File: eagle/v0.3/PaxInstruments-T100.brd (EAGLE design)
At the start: 45.1 x 17.1 mm, 29 parts, among them U1 Attiny85

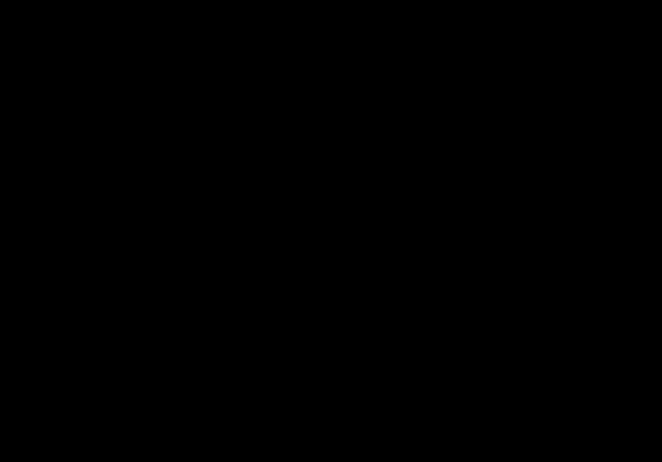
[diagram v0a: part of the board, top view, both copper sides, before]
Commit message: Added indicator LED and breakout header.
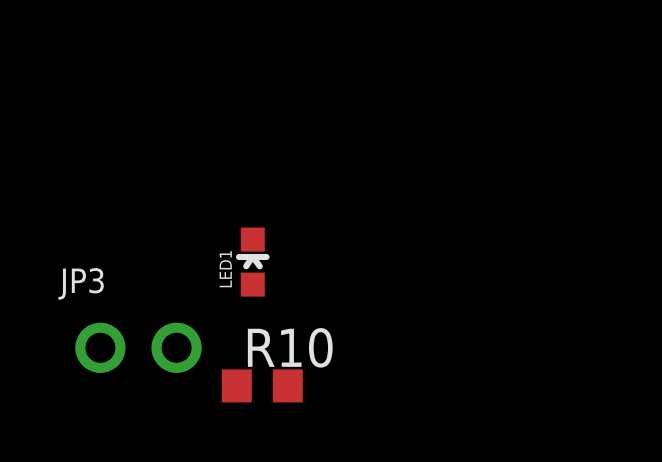
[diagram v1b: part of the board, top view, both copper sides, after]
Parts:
- added JP3: (no value), microbuilder:1X02_ROUND
- added LED1: (no value), SparkFun-LED:LED-0603
- added R10: 500R, rcl:R0603
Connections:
- new net N$5: LED1.A, R10.1
- net GND: now also JP3.1, LED1.C
- net SPARE: now also JP3.2, R10.2
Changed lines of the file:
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@@
 <attribute name="VALUE" x="23.5776" y="15.875" size="0.02" layer="27"/>
 </element>
+<element name="LED1" library="SparkFun-LED" package="LED-0603" value="" x="-16.8275" y="0.9525"/>
+<element name="R10" library="rcl" package="R0603" value="500R" x="-16.51" y="-3.175"/>
+<element name="JP3" library="microbuilder" package="1X02_ROUND" value="" x="-20.6375" y="-1.905"/>
 </elements>
 <signals>
@@
 <contactref element="JP2" pad="6"/>
 <contactref element="SJ1" pad="1"/>
+<contactref element="LED1" pad="C"/>
+<contactref element="JP3" pad="1"/>
+<wire x1="21.2725" y1="11.9625" x2="22.4155" y2="15.875" width="0" layer="19" extent="1-1"/>
+<wire x1="17.8435" y1="10.16" x2="21.2725" y2="11.9625" width="0" layer="19" extent="1-1"/>
+<wire x1="9.7225" y1="8.5725" x2="17.8435" y2="10.16" width="0" layer="19" extent="1-1"/>
+<wire x1="9.7225" y1="12.3825" x2="9.7225" y2="8.5725" width="0" layer="19" extent="1-1"/>
+<wire x1="5.2575" y1="12.0725" x2="9.7225" y2="12.3825" width="0" layer="19" extent="1-1"/>
+<wire x1="12.1793" y1="3.81" x2="9.7225" y2="8.5725" width="0" layer="19" extent="1-1"/>
+<wire x1="9.02" y1="1.905" x2="12.1793" y2="3.81" width="0" layer="19" extent="1-1"/>
+<wire x1="-16.8275" y1="1.7025" x2="5.2575" y2="12.0725" width="0" layer="19" extent="1-1"/>
+<wire x1="-21.9075" y1="-1.905" x2="-16.8275" y2="1.7025" width="0" layer="19" extent="1-1"/>
 </signal>
 <signal name="/RST">
@@
 <wire x1="14.2875" y1="13.97" x2="14.2875" y2="15.24" width="0.254" layer="1"/>
 <wire x1="14.2875" y1="15.24" x2="13.2715" y2="15.24" width="0.254" layer="1"/>
+<contactref element="R10" pad="2"/>
+<contactref element="JP3" pad="2"/>
+<wire x1="-15.66" y1="-3.175" x2="14.2875" y2="5.08" width="0" layer="19" extent="1-1"/>
+<wire x1="-19.3675" y1="-1.905" x2="-15.66" y2="-3.175" width="0" layer="19" extent="1-1"/>
 </signal>
 <signal name="SDA">
@@
 <wire x1="37.846" y1="12.3825" x2="38.1" y2="12.6365" width="0.4064" layer="1"/>
 </signal>
+<signal name="N$5">
+<contactref element="R10" pad="1"/>
+<contactref element="LED1" pad="A"/>
+<wire x1="-16.8275" y1="0.2025" x2="-17.36" y2="-3.175" width="0" layer="19" extent="1-1"/>
+</signal>
 </signals>

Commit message: [V0.3] - initial layout
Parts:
- removed LOGO1: OSHW-LOGOS, SparkFun-Aesthetics:OSHW-LOGO-S
- removed SJ1: (no value), jumper:SJ
- removed U$1: PAX-LOGO, charlespax:PAX-LOGO
- removed U$2: CHARLESPAX_TC-MINI-CONNECTOR, PaxInstrument-T400:CHARLESPAX_TC-MINI-CONNECTOR
- added L2: (no value), SeeesStudio-OPL:L0603
- added U$5: TC-MINI-INSIDE, PaxInstruments-Connectors:TC-CLIP-INSIDE
- moved JP3 33.3 mm to (7.94, 15.2)
- moved R10 29.7 mm to (12.7, 2.22)
- moved LED1 29.5 mm to (12.7, 0.95), turned to 90 degrees
- moved C6 1.59 mm to (29.8, 4.13)
- moved R3 1.59 mm to (29.8, 5.71)
- moved U$4 0.64 mm to (26.0, 12.7)
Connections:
- net AGND: now also L2.2; no longer SJ1.2
- net GND: now also L2.1; no longer SJ1.1
- net N$3: now also U$5.P$2; no longer U$2.P$2
- net N$4: now also U$5.P$1; no longer U$2.P$1
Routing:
- net SPARE: track 15.8 -> 22.9 mm
- net D+: track 15.5 -> 8.89 mm, vias 2 -> 0
- net N$4: track 14.1 -> 10.3 mm
- net SDA: track 35.4 -> 31.7 mm
- net N$5: track 0.00 -> 2.05 mm
- net USB_5V: track 71.4 -> 69.5 mm, vias 3 -> 2
- net TC-: track 7.12 -> 8.86 mm
- net A_5V: track 27.4 -> 28.9 mm
- net N$3: track 13.6 -> 12.4 mm
- net SCL: track 21.8 -> 21.0 mm
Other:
- board size 45.1 x 17.1 mm -> 46 x 17.1 mm
- board text added: "LOGO"

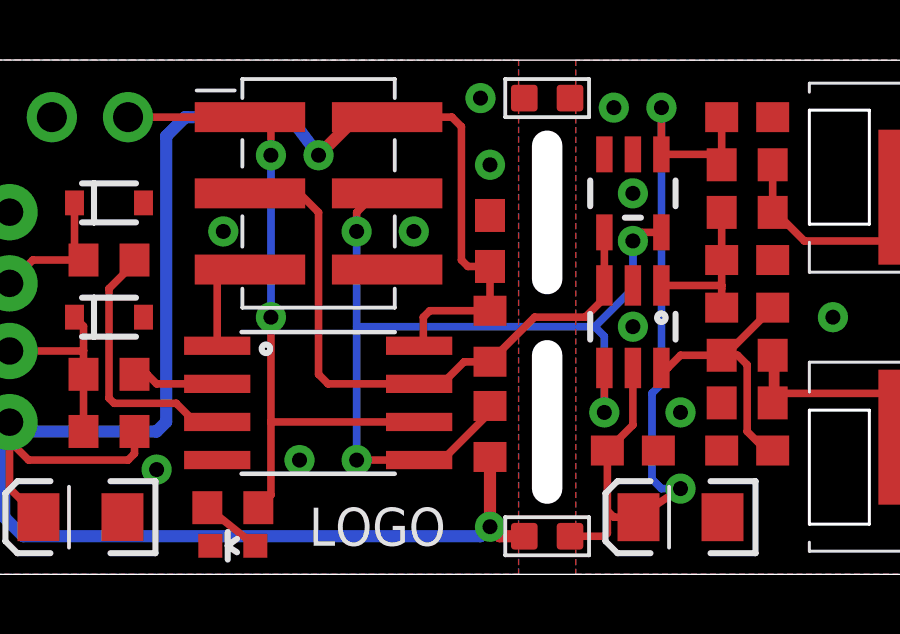
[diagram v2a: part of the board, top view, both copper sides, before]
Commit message: New library added. Inductor changed to resistor. Logo placement.
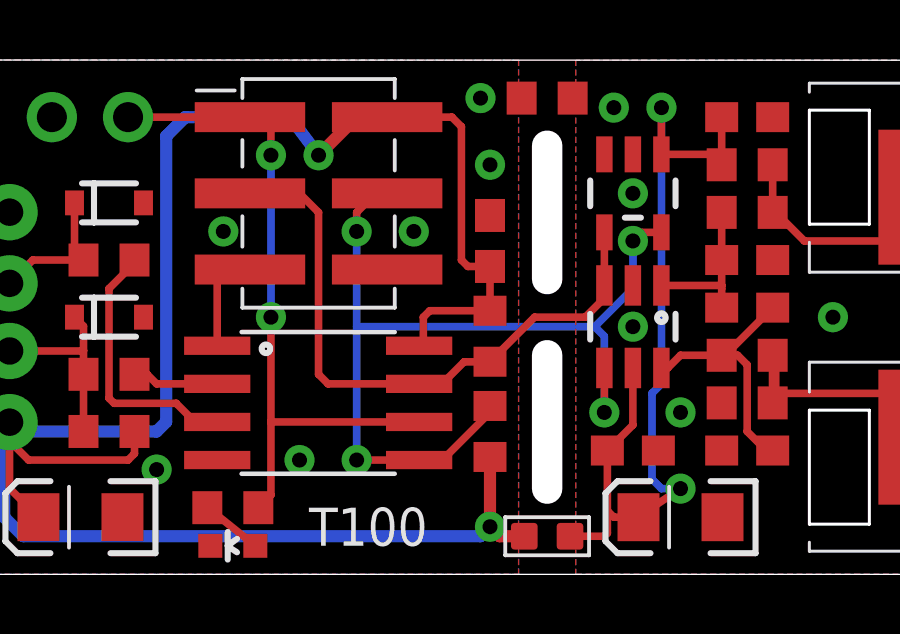
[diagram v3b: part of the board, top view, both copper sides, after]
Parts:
- removed L2: (no value), SeeesStudio-OPL:L0603
- added R11: 0R, rcl:R0603
- added U$1: PAX-LOGOPAX-LOGO-0.25IN, PaxInstruments-Aesthetics:PAX-LOGO-0.25IN
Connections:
- net AGND: now also R11.1; no longer L2.2
- net GND: now also R11.2; no longer L2.1
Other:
- board text added: "T100"
- board text removed: "LOGO"
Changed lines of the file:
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@@
 <text x="45.085" y="18.415" size="1.016" layer="26" font="vector" rot="MR0">Pax Instruments T-100
 [v0.3] x 2014</text>
-<text x="15.24" y="0.9525" size="1.27" layer="25" font="vector">LOGO</text>
+<text x="15.24" y="0.9525" size="1.27" layer="25" font="vector">T100</text>
 </plain>
 <attributes>
@@
 <attribute name="MPN" value="Thermo-clip2" x="38.4175" y="8.5725" size="1.778" layer="27" rot="R270" display="off"/>
 </element>
-<element name="L2" library="SeeesStudio-OPL" package="L0603" value="" x="23.1775" y="15.875" smashed="yes">
-<attribute name="VALUE" x="21.6535" y="15.5575" size="0.635" layer="27" ratio="10"/>
-</element>
+<element name="U$1" library="PaxInstruments-Aesthetics" package="PAX-LOGO-0.25IN" value="PAX-LOGOPAX-LOGO-0.25IN" x="13.0175" y="4.1275" rot="MR0"/>
+<element name="R11" library="rcl" package="R0603" value="0R" x="23.1775" y="15.875" smashed="yes" rot="R180"/>
 </elements>
 <signals>
@@
 <contactref element="LED1" pad="C"/>
 <contactref element="JP3" pad="1"/>
-<contactref element="L2" pad="1"/>
 <via x="18.7325" y="11.43" extent="1-16" drill="0.5"/>
 <via x="21.2725" y="13.6525" extent="1-16" drill="0.5"/>
@@
 <via x="10.16" y="3.4925" extent="1-16" drill="0.5"/>
 <via x="14.9225" y="3.81" extent="1-16" drill="0.5"/>
+<contactref element="R11" pad="2"/>
 </signal>
 <signal name="/RST">
@@
 <contactref element="C6" pad="2"/>
 <contactref element="C7" pad="2"/>
-<contactref element="L2" pad="2"/>
 <via x="43.815" y="8.5725" extent="1-16" drill="0.5"/>
 <via x="26.035" y="12.7" extent="1-16" drill="0.5"/>
@@
 <via x="32.7025" y="8.5725" extent="1-16" drill="0.5"/>
 <via x="38.4175" y="8.5725" extent="1-16" drill="0.5"/>
+<contactref element="R11" pad="1"/>
 </signal>
 <signal name="TC+">

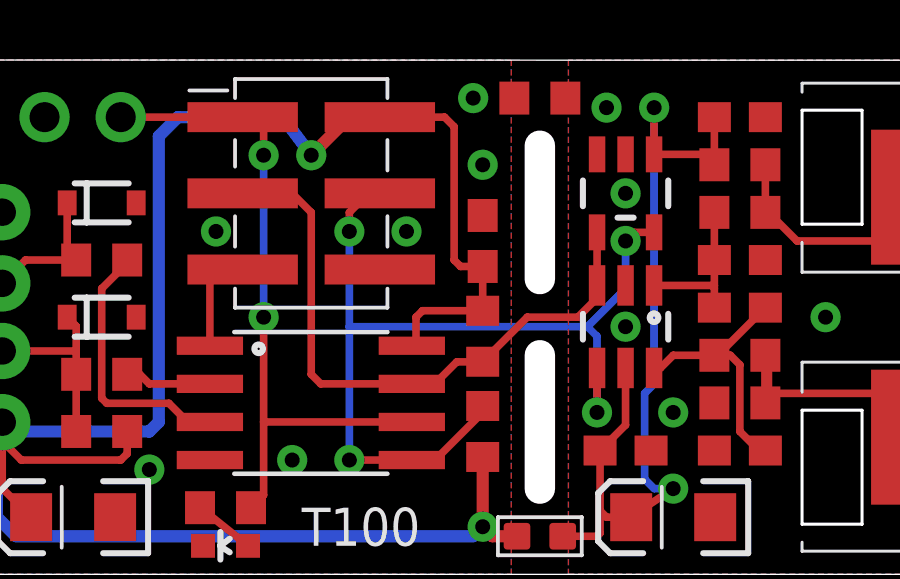
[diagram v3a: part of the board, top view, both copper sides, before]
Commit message: Text label placements.
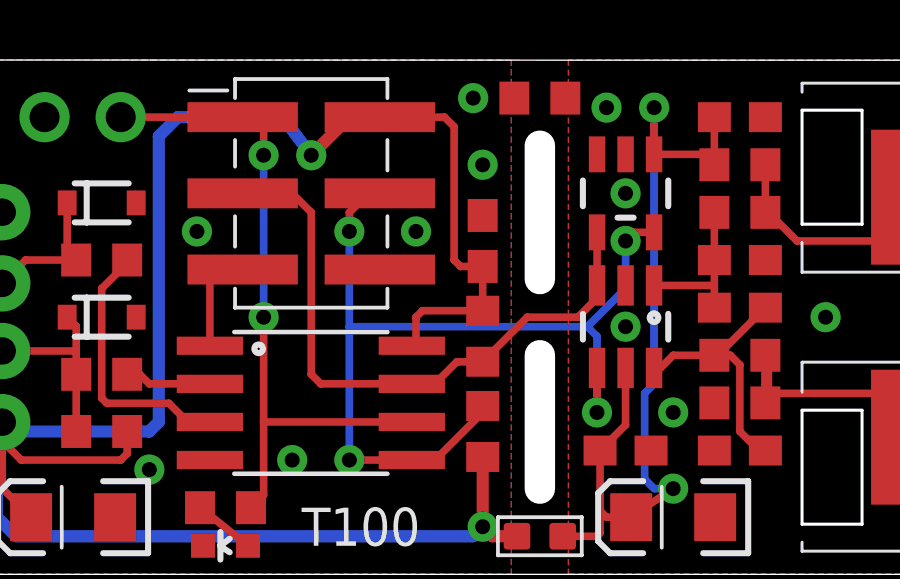
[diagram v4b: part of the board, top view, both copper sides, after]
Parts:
- added LOGO1: SPARKFUN-AESTHETICS_OSHW-LOGOS, PaxInstrument-T400:SPARKFUN-AESTHETICS_OSHW-LOGO-S
- moved U$1 9.34 mm to (20.6, 9.53)
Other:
- board text added: "Pax Instruments Temperature LabStick T100 v0.3 beta"
- board text added: "paxinstruments.com/ products/sku2252"
- board text removed: "Pax Instruments T-100 [v0.3] x 2014"
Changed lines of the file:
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@@
 <wire x1="23.1775" y1="14.2875" x2="23.1775" y2="9.8425" width="1.016" layer="46"/>
 <wire x1="23.1775" y1="7.3025" x2="23.1775" y2="2.8575" width="1.016" layer="46"/>
-<text x="45.085" y="18.415" size="1.016" layer="26" font="vector" rot="MR0">Pax Instruments T-100
-[v0.3] x 2014</text>
+<text x="20.6375" y="4.445" size="0.889" layer="26" font="vector" rot="MR0">Pax Instruments
+Temperature LabStick
+T100 v0.3 beta</text>
 <text x="15.24" y="0.9525" size="1.27" layer="25" font="vector">T100</text>
+<text x="20.6375" y="0.635" size="0.889" layer="26" font="vector" rot="MR0">paxinstruments.com/
+products/sku2252</text>
 </plain>
 <attributes>
@@
 <attribute name="MPN" value="Thermo-clip2" x="38.4175" y="8.5725" size="1.778" layer="27" rot="R270" display="off"/>
 </element>
-<element name="U$1" library="PaxInstruments-Aesthetics" package="PAX-LOGO-0.25IN" value="PAX-LOGOPAX-LOGO-0.25IN" x="13.0175" y="4.1275" rot="MR0"/>
+<element name="U$1" library="PaxInstruments-Aesthetics" package="PAX-LOGO-0.25IN" value="PAX-LOGOPAX-LOGO-0.25IN" x="20.6375" y="9.525" rot="MR0"/>
 <element name="R11" library="rcl" package="R0603" value="0R" x="23.1775" y="15.875" smashed="yes" rot="R180"/>
+<element name="LOGO1" library="PaxInstrument-T400" package="SPARKFUN-AESTHETICS_OSHW-LOGO-S" value="SPARKFUN-AESTHETICS_OSHW-LOGOS" x="38.4175" y="4.445" rot="MR0"/>
 </elements>
 <signals>
@@
 <contactref element="LED1" pad="C"/>
 <contactref element="JP3" pad="1"/>
-<via x="18.7325" y="11.43" extent="1-16" drill="0.5"/>
+<via x="19.05" y="11.43" extent="1-16" drill="0.5"/>
 <via x="21.2725" y="13.6525" extent="1-16" drill="0.5"/>
 <via x="20.955" y="15.875" extent="1-16" drill="0.5"/>
-<via x="12.3825" y="11.43" extent="1-16" drill="0.5"/>
+<via x="11.7475" y="11.43" extent="1-16" drill="0.5"/>
 <via x="10.16" y="3.4925" extent="1-16" drill="0.5"/>
 <via x="14.9225" y="3.81" extent="1-16" drill="0.5"/>
@@
 <contactref element="C7" pad="1"/>
 <wire x1="28.995" y1="12.065" x2="28.995" y2="10.4775" width="0.254" layer="1"/>
-<wire x1="28.995" y1="8.89" x2="28.995" y2="9.525" width="0.254" layer="1"/>
+<wire x1="28.995" y1="8.89" x2="28.995" y2="9.6301" width="0.254" layer="1"/>
 <wire x1="28.995" y1="9.6301" x2="28.995" y2="10.4775" width="0.254" layer="1"/>
 <wire x1="26.985" y1="9.6301" x2="28.995" y2="9.6301" width="0.254" layer="1"/>
-<wire x1="28.995" y1="9.6301" x2="28.995" y2="9.525" width="0.254" layer="1"/>
 </signal>
 <signal name="TC-">

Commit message: Added MCP9800A0 part number. Closes #47.
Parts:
- U$4: value MCP9800 -> MCP9800A0
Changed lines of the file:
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@@
 <?xml version="1.0" encoding="utf-8"?>
 <!DOCTYPE eagle SYSTEM "eagle.dtd">
-<eagle version="7.3.0">
+<eagle version="7.2.0">
 <drawing>
 <settings>
@@
 </element>
 <element name="U$3" library="SparkFun-DigitalIC" package="SOT23-6" value="MCP3421" x="26.035" y="8.255" smashed="yes" rot="R180"/>
-<element name="U$4" library="SparkFun-DigitalIC" package="SOT23-5" value="MCP9800" x="26.035" y="12.7" smashed="yes" rot="R180"/>
+<element name="U$4" library="SparkFun-DigitalIC" package="SOT23-5" value="MCP9800A0" x="26.035" y="12.7" smashed="yes" rot="R180"/>
 <element name="L1" library="SeeesStudio-OPL" package="L0603" value="" x="23.1775" y="1.27" smashed="yes">
 <attribute name="VALUE" x="21.6535" y="0.9525" size="0.635" layer="27" ratio="10"/>

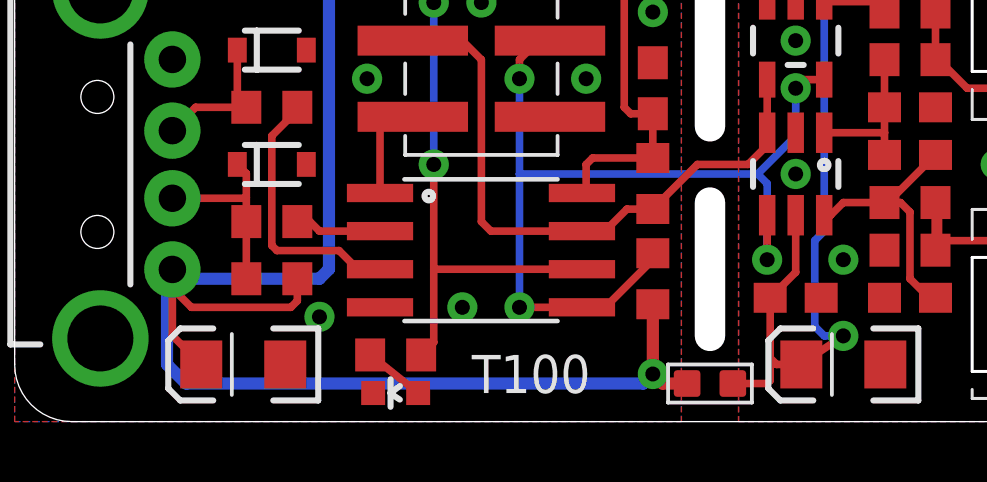
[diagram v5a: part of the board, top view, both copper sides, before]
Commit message: Added a bunch of BoM data.
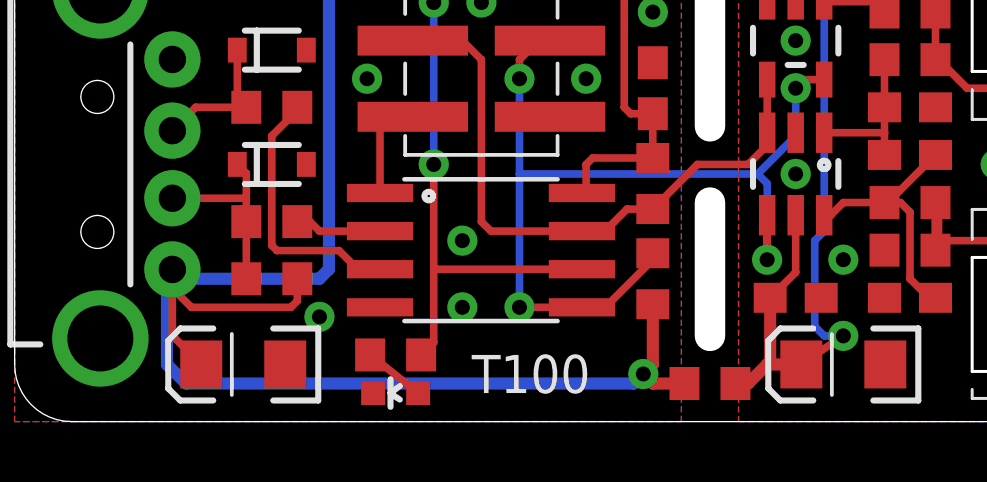
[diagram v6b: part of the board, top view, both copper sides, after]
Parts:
- removed L1: (no value), SeeesStudio-OPL:L0603
- removed LOGO1: SPARKFUN-AESTHETICS_OSHW-LOGOS, PaxInstrument-T400:SPARKFUN-AESTHETICS_OSHW-LOGO-S
- added R12: 0R, rcl:R0603
- LED1: value (none) -> Green
- U$3: value MCP3421 -> MCP3421A0
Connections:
- net A_5V: now also R12.1; no longer L1.2
- net USB_5V: now also R12.2; no longer L1.1

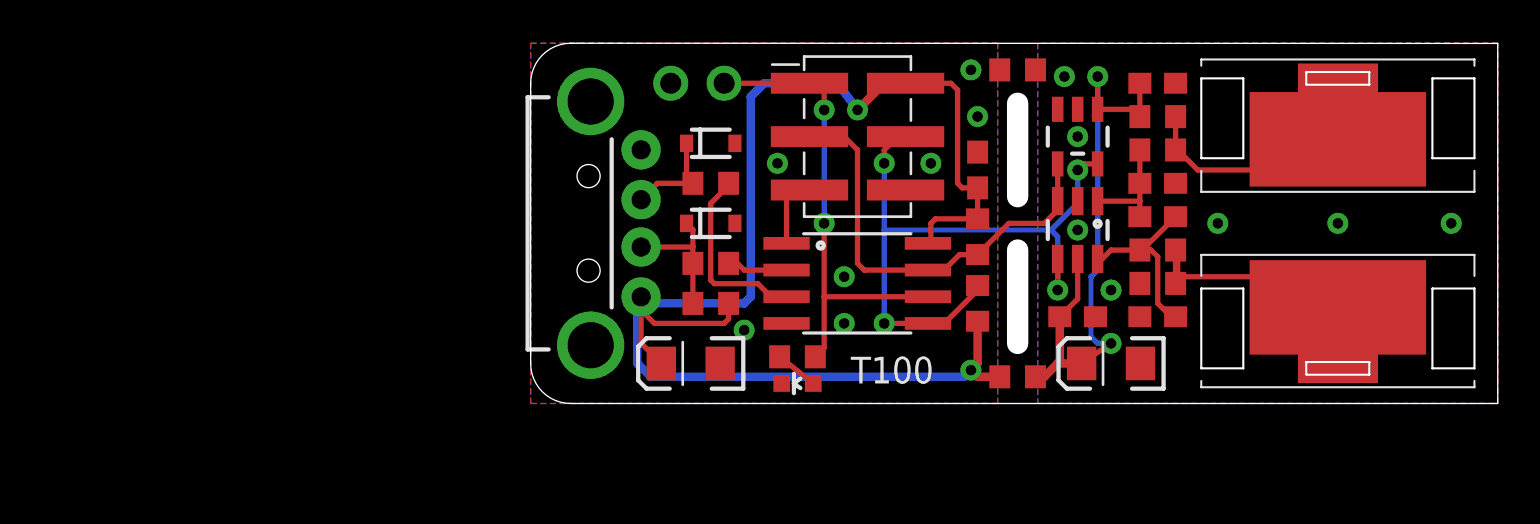
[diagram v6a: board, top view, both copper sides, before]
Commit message: Updated thermocoupel connector. Moved MCP9800 to between the thermocouple connectors. BoM should be finished.
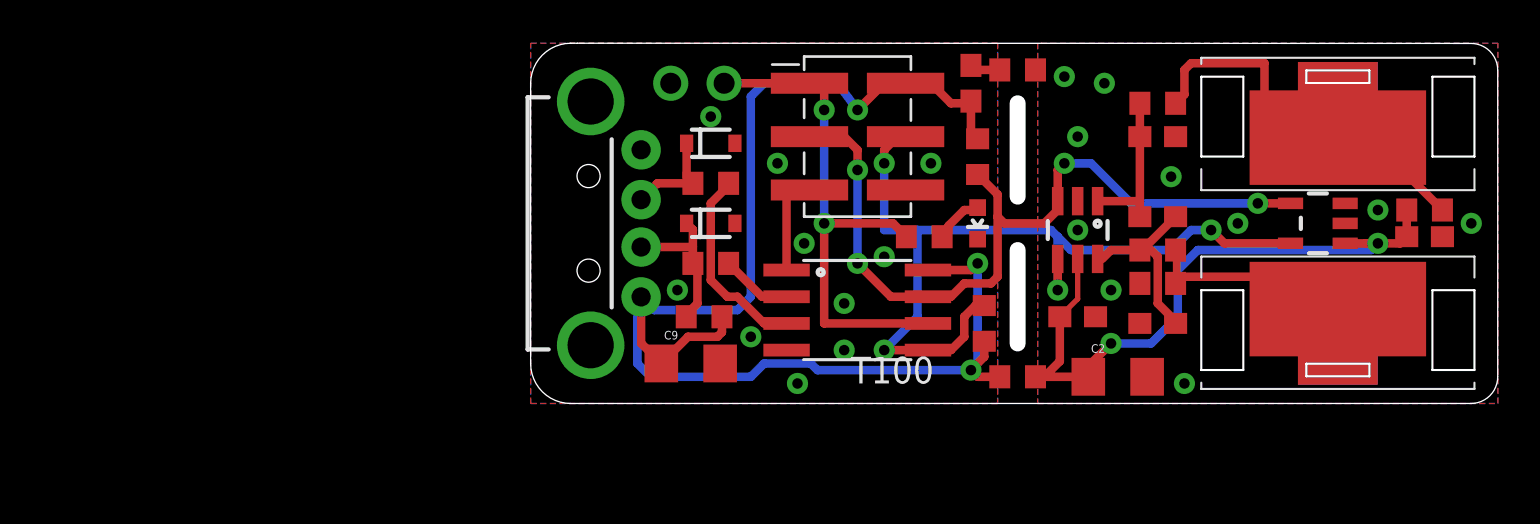
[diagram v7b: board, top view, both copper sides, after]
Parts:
- removed C3: 10uF, SparkFun-Capacitors:EIA3216
- removed U$5: TC-MINI-INSIDE, PaxInstruments-Connectors:TC-CLIP-INSIDE
- added C9: 10uF, SparkFun-Passives:1206
- added U$2, U$6: TC-MINI-SINGLE, PaxInstruments-Connectors:TC-CLIP-SINGLE
- C2: device SparkFun-Capacitors:EIA3216 -> SparkFun-Passives:1206
- R10, R5, R6: value 500R -> 499R
- moved C2 20.3 mm to (27.9, 1.27), turned to 0 degrees
- moved C5 14.6 mm to (42.5, 7.94)
- moved R4 13.5 mm to (42.5, 9.21)
- moved U$4 12.2 mm to (37.5, 8.57), turned to 90 degrees
- moved LED1 11.5 mm to (21.3, 8.57), turned to 180 degrees
- moved R10 8.31 mm to (18.7, 7.94), turned to 180 degrees
- moved C1 4.14 mm to (21.0, 15.2)
- moved R8 3.81 mm to (21.3, 11.7)
- moved C7 2.22 mm to (29.8, 12.7)
- moved R6 2.22 mm to (29.8, 14.3)
- moved U1 1.27 mm to (15.6, 4.45)
- moved R7 1.00 mm to (21.6, 3.81)
- moved R9 0.71 mm to (8.26, 4.13)
- moved C6 0.32 mm to (29.8, 3.81)
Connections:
- net AGND: now also C2.2; no longer C3.C
- net A_5V: now also C2.1; no longer C3.A
- net GND: now also C9.2; no longer C2.C
- net N$3: now also U$2.P$1; no longer U$5.P$2
- net N$4: now also U$6.P$1; no longer U$5.P$1
- net USB_5V: now also C9.1; no longer C2.A
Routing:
- net SCL: track 21.0 -> 38.1 mm, vias 0 -> 4
- net SDA: track 31.7 -> 42.1 mm
- net N$4: track 10.3 -> 19.1 mm
- net A_5V: track 28.4 -> 31.5 mm
- net SPARE: track 22.9 -> 25.3 mm
- net TC+: track 5.19 -> 7.41 mm
- net GND: track 0.00 -> 1.46 mm, vias 7 -> 10
- net /RST: track 3.51 -> 4.78 mm
- net N$1: track 6.40 -> 7.35 mm
- net USB_5V: track 69.4 -> 68.5 mm, vias 2 -> 3
- net D-: track 2.89 -> 3.41 mm
- net D+: track 8.89 -> 9.42 mm
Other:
- outline, holes or cut-outs redrawn
